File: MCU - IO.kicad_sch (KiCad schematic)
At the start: 1 part, among them U1 STM32H743ZIT6TR

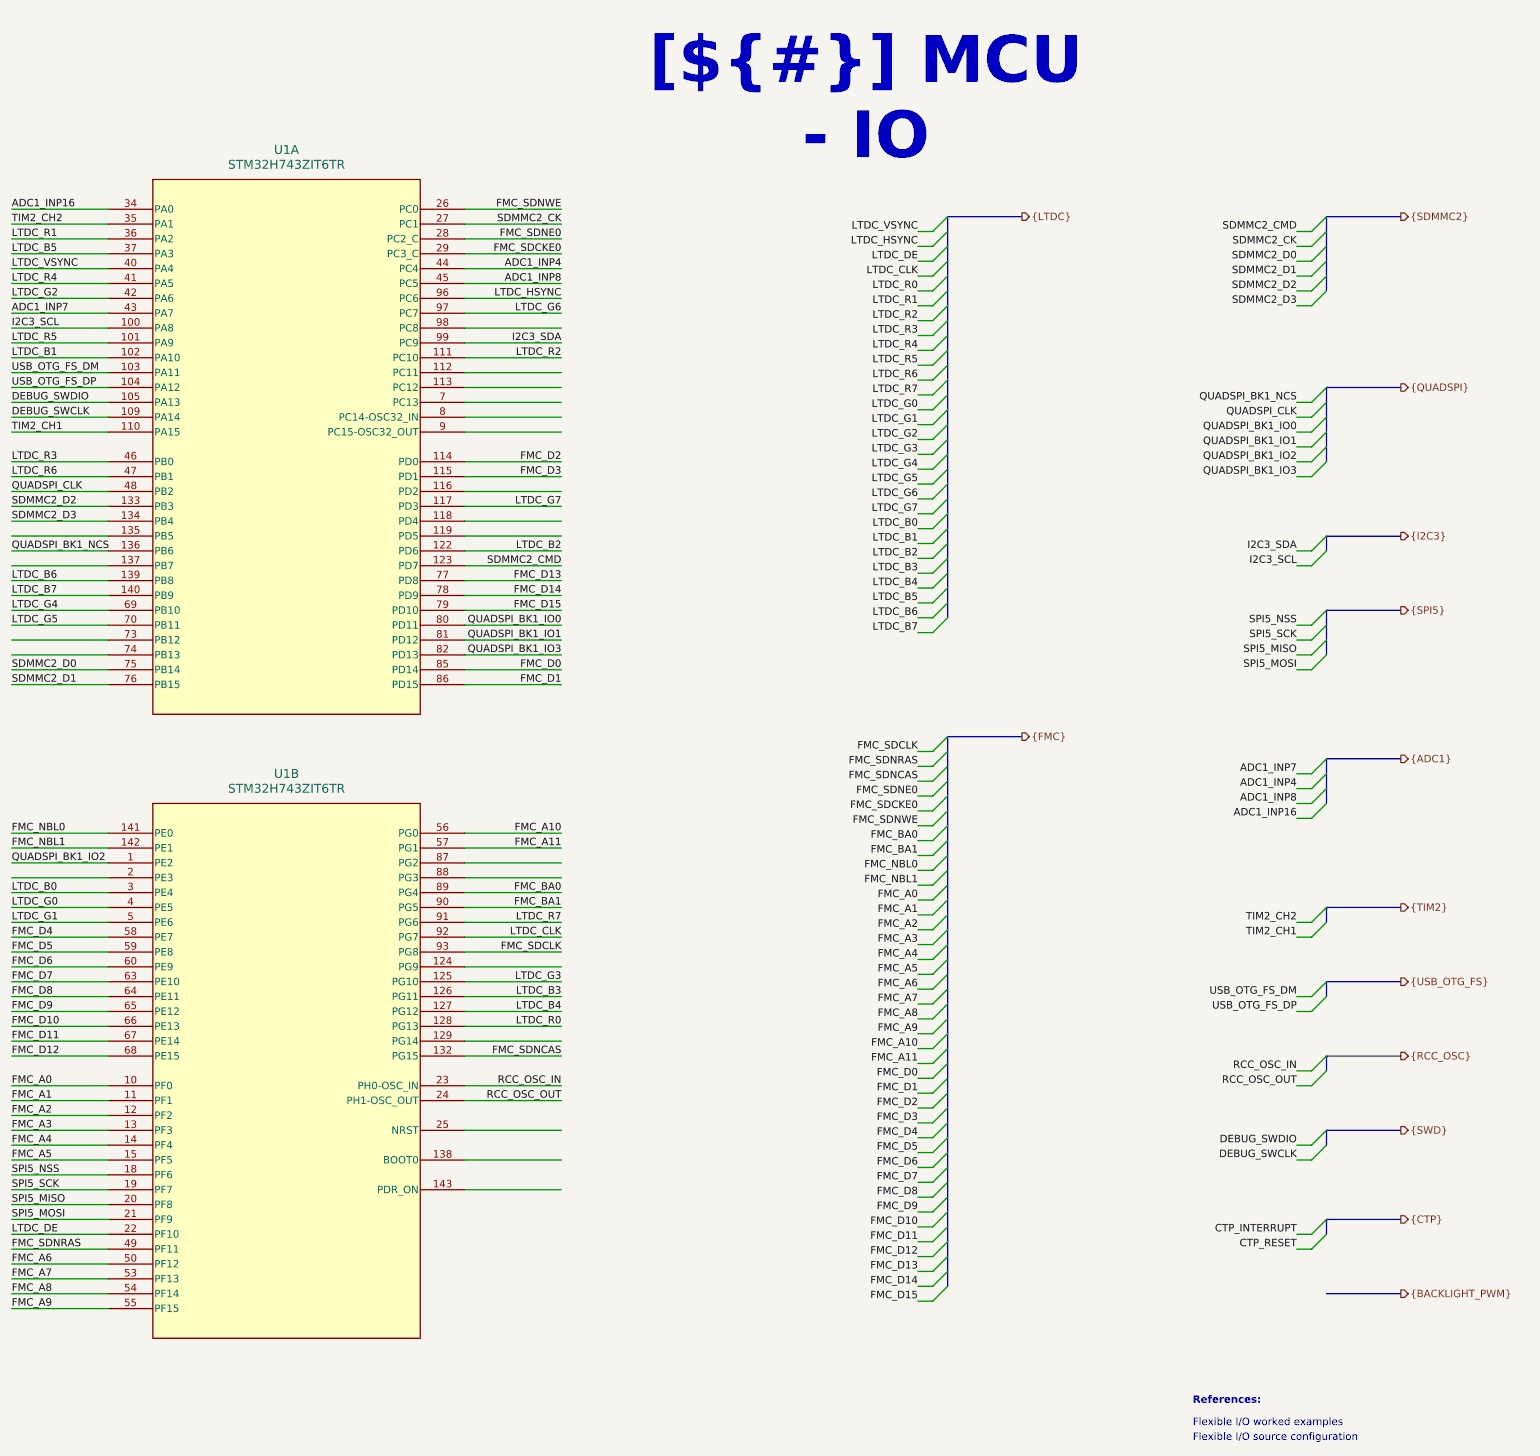
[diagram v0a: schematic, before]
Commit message: added RF ransceiver
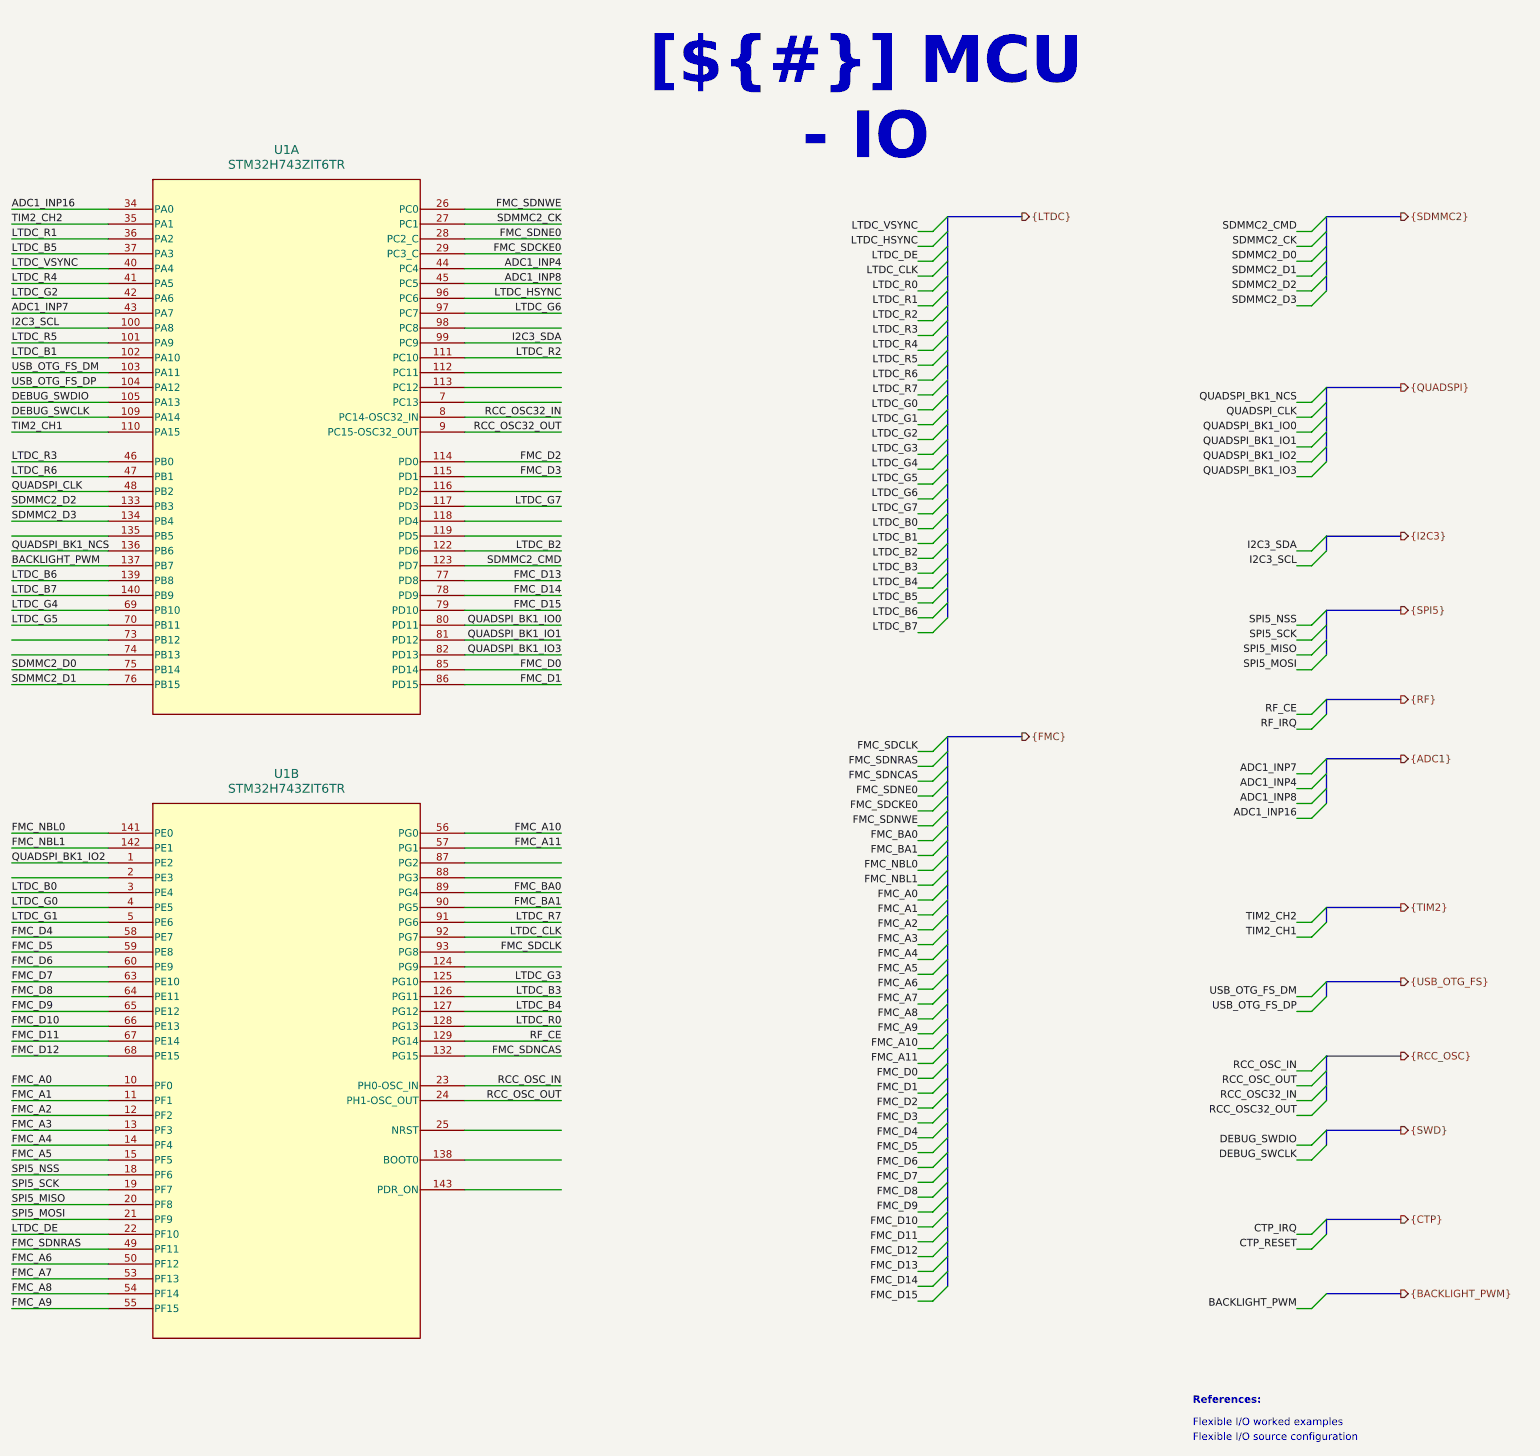
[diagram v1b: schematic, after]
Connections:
- net BACKLIGHT_PWM: now reaches U1.137 (PB7)
- net RCC_OSC32_IN: now reaches U1.8 (PC14-OSC32_IN)
- net RCC_OSC32_OUT: now reaches U1.9 (PC15-OSC32_OUT)
- net RF_CE: now reaches U1.129 (PG14)
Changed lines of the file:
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@@
 		(members "RCC_OSC_IN" "RCC_OSC_OUT")
 	)
+	(bus_alias "RF"
+		(members "RF_IRQ" "RF_CE")
+	)
 	(bus_alias "SDMMC2"
 		(members "SDMMC2_CMD" "SDMMC2_CK" "SDMMC2_D[0..3]")
@@
 	)
 	(bus_entry
+		(at 285.75 233.68)
+		(size 2.54 -2.54)
+		(stroke
+			(width 0)
+			(type default)
+		)
+	)
+	(bus_entry
 		(at 285.75 180.34)
 		(size 2.54 -2.54)
@@
 	)
 	(bus_entry
+		(at 285.75 200.66)
+		(size 2.54 -2.54)
+		(stroke
+			(width 0)
+			(type default)
+		)
+	)
+	(bus_entry
 		(at 220.98 74.93)
 		(size 2.54 -2.54)
@@
 	)
 	(bus_entry
+		(at 285.75 198.12)
+		(size 2.54 -2.54)
+		(stroke
+			(width 0)
+			(type default)
+		)
+	)
+	(bus_entry
 		(at 285.75 142.24)
 		(size 2.54 -2.54)
@@
 	)
 	(bus_entry
+		(at 285.75 134.62)
+		(size 2.54 -2.54)
+		(stroke
+			(width 0)
+			(type default)
+		)
+	)
+	(bus_entry
 		(at 220.98 181.61)
 		(size 2.54 -2.54)
@@
 	)
 	(bus_entry
+		(at 285.75 132.08)
+		(size 2.54 -2.54)
+		(stroke
+			(width 0)
+			(type default)
+		)
+	)
+	(bus_entry
 		(at 220.98 168.91)
 		(size 2.54 -2.54)
@@
 	(wire
 		(pts
+			(xy 283.21 233.68) (xy 285.75 233.68)
+		)
+		(stroke
+			(width 0)
+			(type default)
+		)
+	)
+	(wire
+		(pts
 			(xy 218.44 80.01) (xy 220.98 80.01)
 		)
@@
 		)
 	)
+	(wire
+		(pts
+			(xy 283.21 134.62) (xy 285.75 134.62)
+		)
+		(stroke
+			(width 0)
+			(type default)
+		)
+	)
 	(bus
 		(pts
@@
 	(bus
 		(pts
+			(xy 288.29 129.54) (xy 300.99 129.54)
+		)
+		(stroke
+			(width 0)
+			(type default)
+		)
+	)
+	(bus
+		(pts
 			(xy 223.52 166.37) (xy 223.52 168.91)
 		)
@@
 		)
 	)
+	(wire
+		(pts
+			(xy 283.21 200.66) (xy 285.75 200.66)
+		)
+		(stroke
+			(width 0)
+			(type default)
+		)
+	)
 	(bus
 		(pts
@@
 	(wire
 		(pts
+			(xy 283.21 198.12) (xy 285.75 198.12)
+		)
+		(stroke
+			(width 0)
+			(type default)
+		)
+	)
+	(wire
+		(pts
 			(xy 283.21 180.34) (xy 285.75 180.34)
 		)
@@
 		)
 	)
+	(bus
+		(pts
+			(xy 288.29 193.04) (xy 288.29 195.58)
+		)
+		(stroke
+			(width 0)
+			(type default)
+		)
+	)
 	(wire
 		(pts
@@
 	(wire
 		(pts
+			(xy 283.21 132.08) (xy 285.75 132.08)
+		)
+		(stroke
+			(width 0)
+			(type default)
+		)
+	)
+	(wire
+		(pts
 			(xy 283.21 147.32) (xy 285.75 147.32)
 		)
@@
 		)
 	)
+	(bus
+		(pts
+			(xy 288.29 195.58) (xy 288.29 198.12)
+		)
+		(stroke
+			(width 0)
+			(type default)
+		)
+	)
 	(wire
 		(pts
@@
 	(bus
 		(pts
+			(xy 288.29 129.54) (xy 288.29 132.08)
+		)
+		(stroke
+			(width 0)
+			(type default)
+		)
+	)
+	(bus
+		(pts
 			(xy 288.29 139.7) (xy 288.29 142.24)
 		)
@@
 		)
 	)
+	(label "RF_CE"
+		(at 157.48 187.96 180)
+		(effects
+			(font
+				(size 1.27 1.27)
+			)
+			(justify right bottom)
+		)
+	)
 	(label "LTDC_B2"
 		(at 157.48 104.14 180)
@@
 		)
 	)
+	(label "RCC_OSC32_IN"
+		(at 157.48 81.28 180)
+		(effects
+			(font
+				(size 1.27 1.27)
+			)
+			(justify right bottom)
+		)
+	)
 	(label "FMC_D4"
 		(at 63.5 170.18 0)
@@
 		)
 	)
+	(label "RCC_OSC32_OUT"
+		(at 283.21 200.66 180)
+		(effects
+			(font
+				(size 1.27 1.27)
+			)
+			(justify right bottom)
+		)
+	)
 	(label "LTDC_VSYNC"
 		(at 218.44 49.53 180)
@@
 		)
 	)
+	(label "RF_IRQ"
+		(at 283.21 134.62 180)
+		(effects
+			(font
+				(size 1.27 1.27)
+			)
+			(justify right bottom)
+		)
+	)
 	(label "LTDC_R0"
 		(at 157.48 185.42 180)
@@
 		)
 	)
-	(label "CTP_INTERRUPT"
+	(label "CTP_IRQ"
 		(at 283.21 220.98 180)
 		(effects
@@
 		)
 	)
+	(label "BACKLIGHT_PWM"
+		(at 63.5 106.68 0)
+		(effects
+			(font
+				(size 1.27 1.27)
+			)
+			(justify left bottom)
+		)
+	)
 	(label "I2C3_SDA"
 		(at 283.21 104.14 180)
@@
 		)
 	)
+	(label "RCC_OSC32_IN"
+		(at 283.21 198.12 180)
+		(effects
+			(font
+				(size 1.27 1.27)
+			)
+			(justify right bottom)
+		)
+	)
 	(label "LTDC_G0"
 		(at 63.5 165.1 0)
@@
 		)
 	)
+	(label "RCC_OSC32_OUT"
+		(at 157.48 83.82 180)
+		(effects
+			(font
+				(size 1.27 1.27)
+			)
+			(justify right bottom)
+		)
+	)
 	(label "QUADSPI_BK1_IO3"
 		(at 157.48 121.92 180)
@@
 		)
 	)
+	(label "BACKLIGHT_PWM"
+		(at 283.21 233.68 180)
+		(effects
+			(font
+				(size 1.27 1.27)
+			)
+			(justify right bottom)
+		)
+	)
 	(label "FMC_SDNE0"
 		(at 218.44 146.05 180)
@@
 		)
 	)
+	(label "RF_CE"
+		(at 283.21 132.08 180)
+		(effects
+			(font
+				(size 1.27 1.27)
+			)
+			(justify right bottom)
+		)
+	)
 	(label "QUADSPI_BK1_IO3"
 		(at 283.21 91.44 180)
@@
 		(effects
 			(font
+				(size 1.27 1.27)
+			)
+			(justify left)
+		)
+	)
+	(hierarchical_label "{RF}"
+		(shape output)
+		(at 300.99 129.54 0)
+		(effects
+			(font

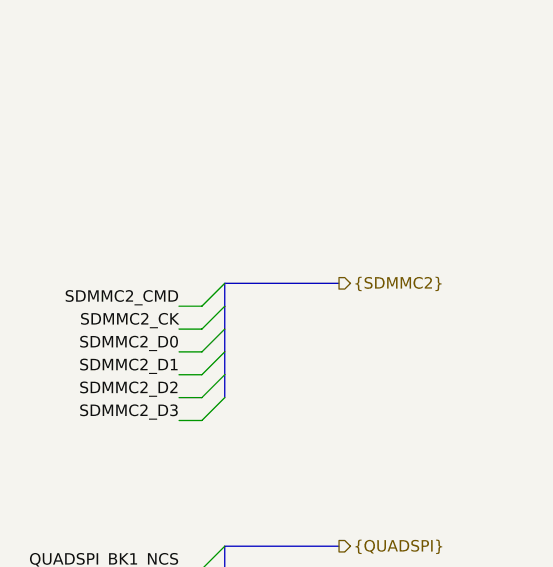
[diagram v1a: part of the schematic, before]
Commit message: added sd card schematic and refactor page numbers and general tab
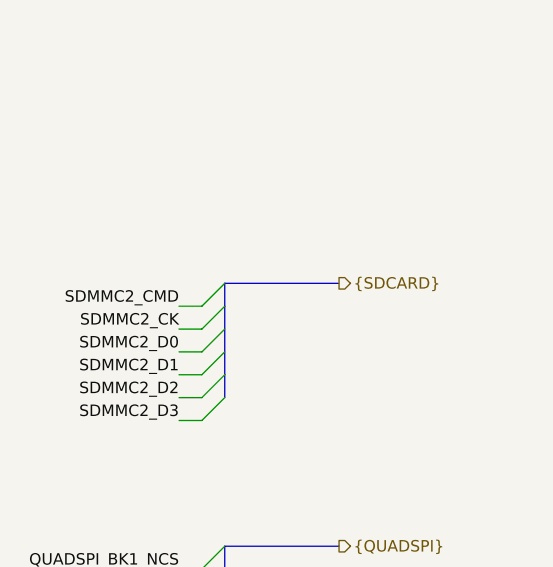
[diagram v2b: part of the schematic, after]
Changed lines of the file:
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@@
 		(members "RF_IRQ" "RF_CE")
 	)
-	(bus_alias "SDMMC2"
-		(members "SDMMC2_CMD" "SDMMC2_CK" "SDMMC2_D[0..3]")
+	(bus_alias "SDCARD"
+		(members "SDMMC2_CMD" "SDMMC2_CK" "SDMMC2_D[0..3]" "CD")
 	)
 	(bus_alias "SPI5"
@@
 		)
 	)
-	(hierarchical_label "{SDMMC2}"
+	(hierarchical_label "{SDCARD}"
 		(shape output)
 		(at 300.99 46.99 0)

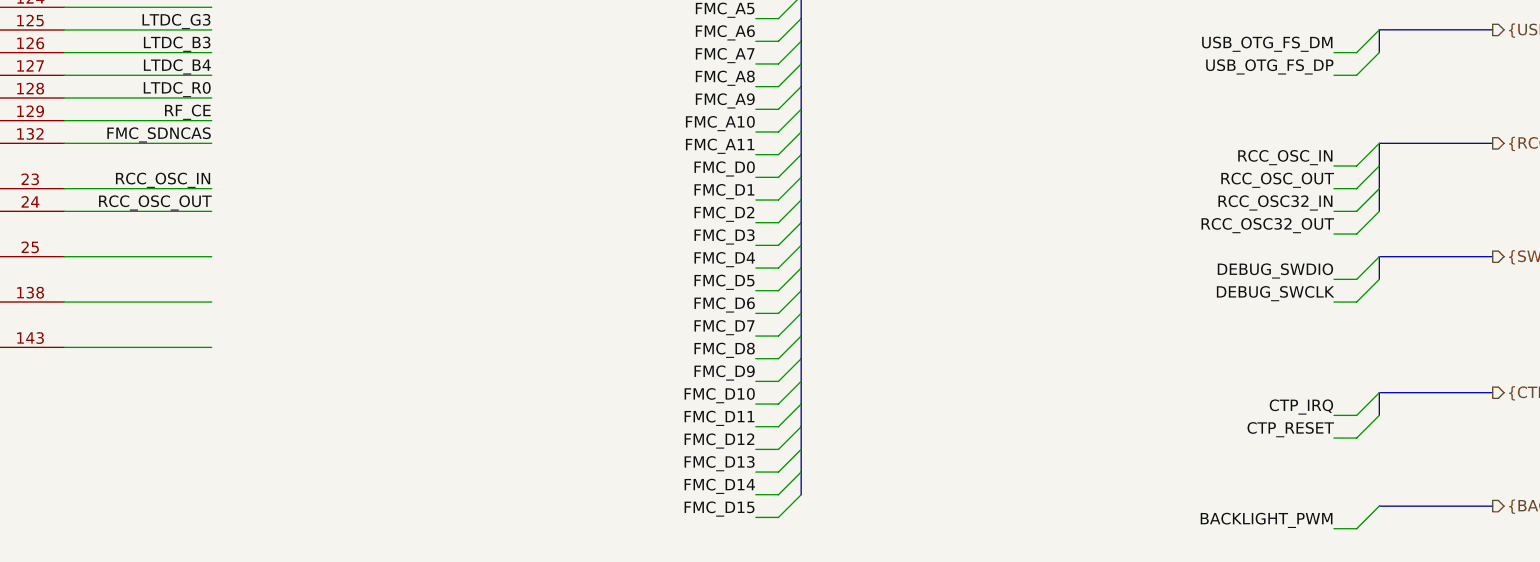
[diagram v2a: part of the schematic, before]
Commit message: added auxiliary schematic, problem with kicad - cannot modify project settings
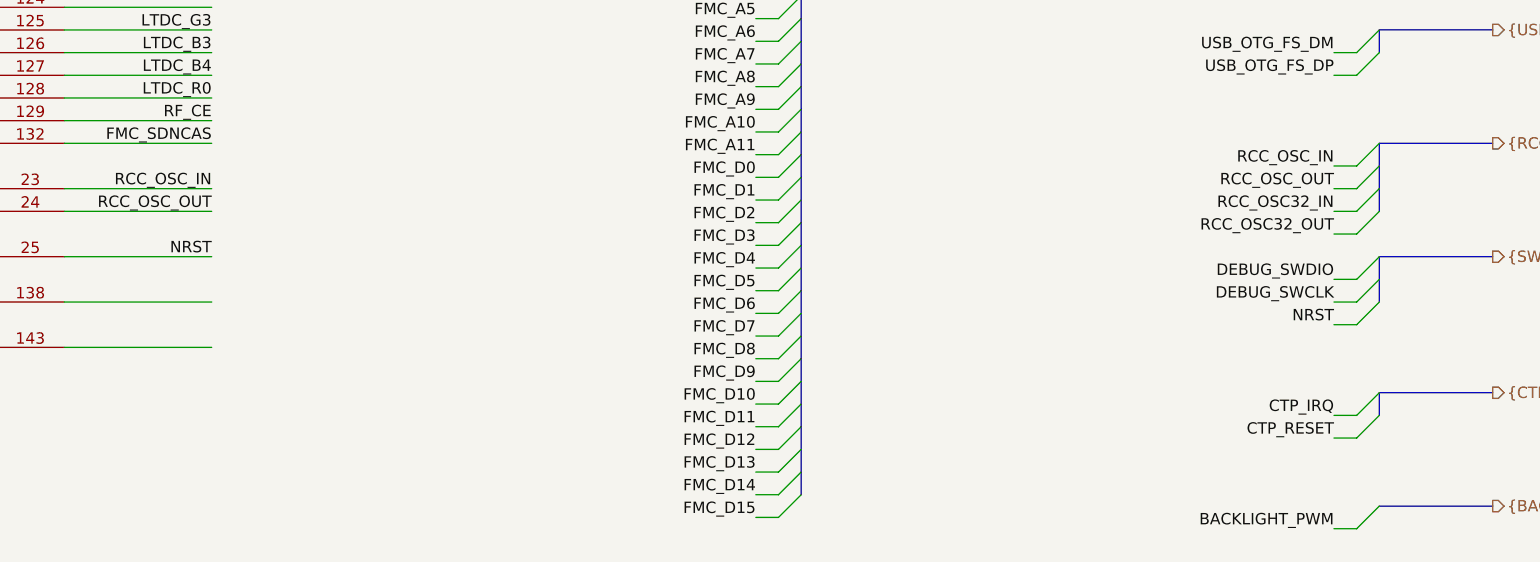
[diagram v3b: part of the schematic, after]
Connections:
- net NRST: now reaches U1.25 (NRST)
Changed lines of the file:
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@@
 	)
 	(bus_entry
+		(at 285.75 210.82)
+		(size 2.54 -2.54)
+		(stroke
+			(width 0)
+			(type default)
+		)
+	)
+	(bus_entry
 		(at 220.98 184.15)
 		(size 2.54 -2.54)
@@
 	(bus
 		(pts
+			(xy 288.29 205.74) (xy 288.29 208.28)
+		)
+		(stroke
+			(width 0)
+			(type default)
+		)
+	)
+	(bus
+		(pts
 			(xy 223.52 107.95) (xy 223.52 110.49)
 		)
@@
 	(wire
 		(pts
+			(xy 283.21 210.82) (xy 285.75 210.82)
+		)
+		(stroke
+			(width 0)
+			(type default)
+		)
+	)
+	(wire
+		(pts
 			(xy 218.44 176.53) (xy 220.98 176.53)
 		)
@@
 		)
 	)
+	(label "NRST"
+		(at 283.21 210.82 180)
+		(effects
+			(font
+				(size 1.27 1.27)
+			)
+			(justify right bottom)
+		)
+	)
 	(label "QUADSPI_BK1_IO3"
 		(at 157.48 121.92 180)
@@
 		(effects
 			(font
+				(size 1.27 1.27)
+			)
+			(justify right bottom)
+		)
+	)
+	(label "NRST"
+		(at 157.48 203.2 180)
+		(effects
+			(font
